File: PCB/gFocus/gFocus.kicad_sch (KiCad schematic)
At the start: 49 parts, among them J1 FTSH-105-01-F-DV-P-TR, J2 Conn_Coaxial, J3 Conn_02x06_Counter_Clockwise, J4 USB_B_Micro, U1 NMA0515SC, U2 TPS7A3001DGNT, U3 TPS7A4901DGNR, U4 AD5761RBRUZ-RL7, U5 ATSAMD21G18A-A, U6 IP4234CZ6, U8 LDK130-32_SOT23_SOT353

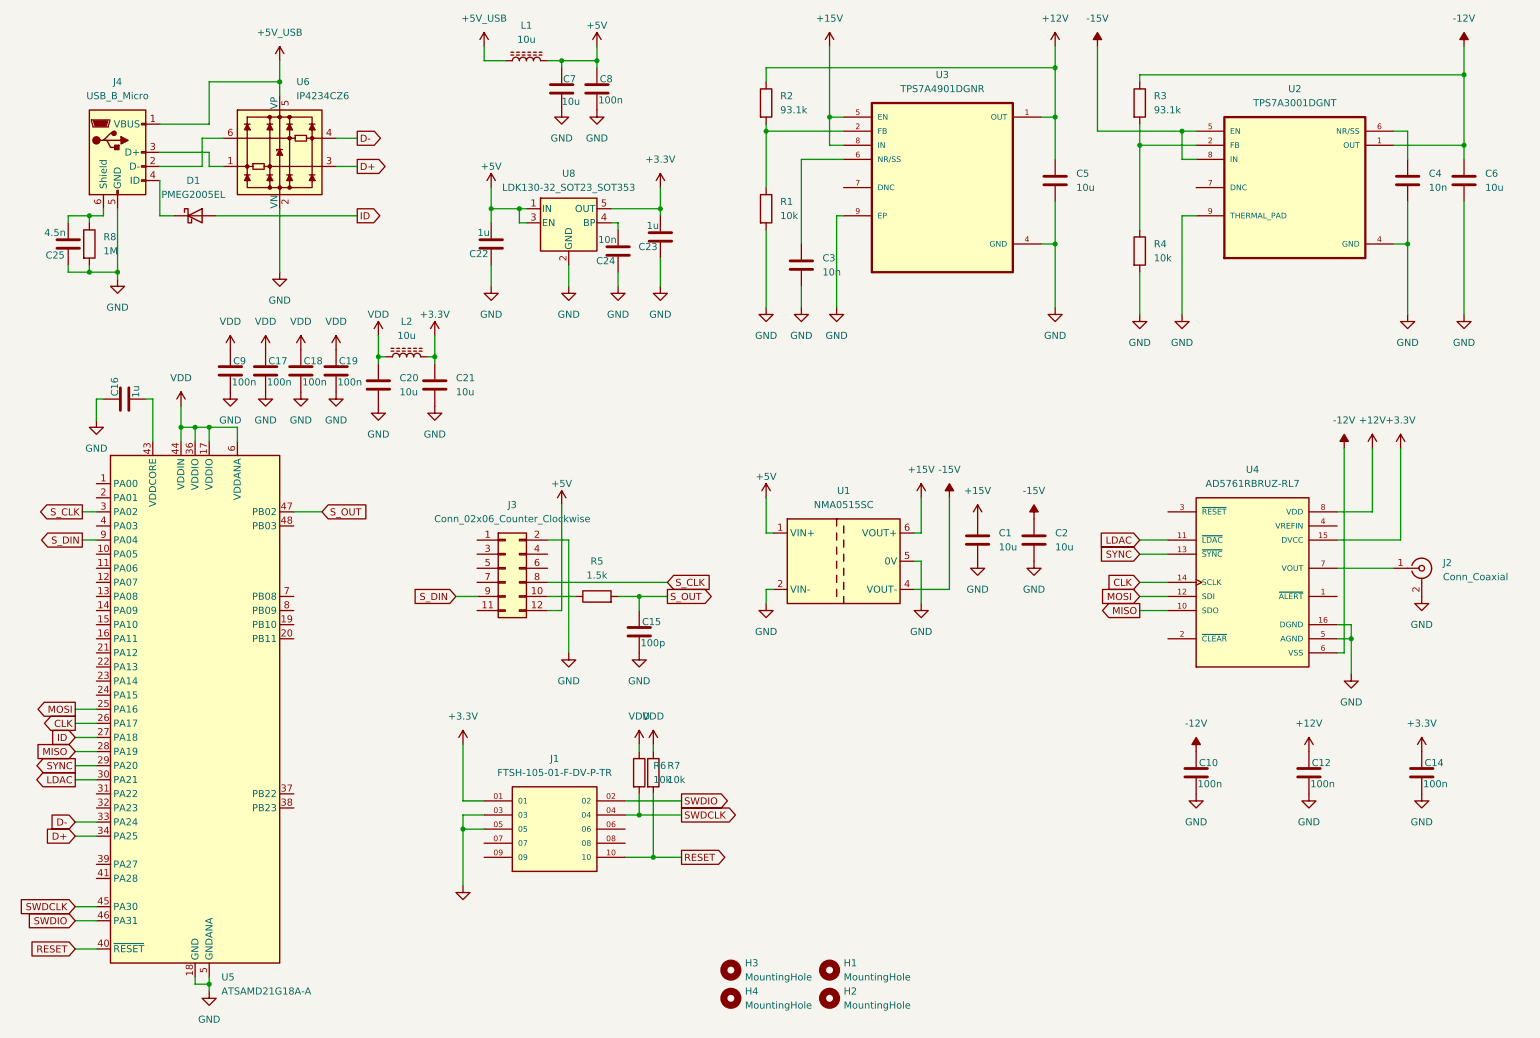
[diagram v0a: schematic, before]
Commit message: added drivers
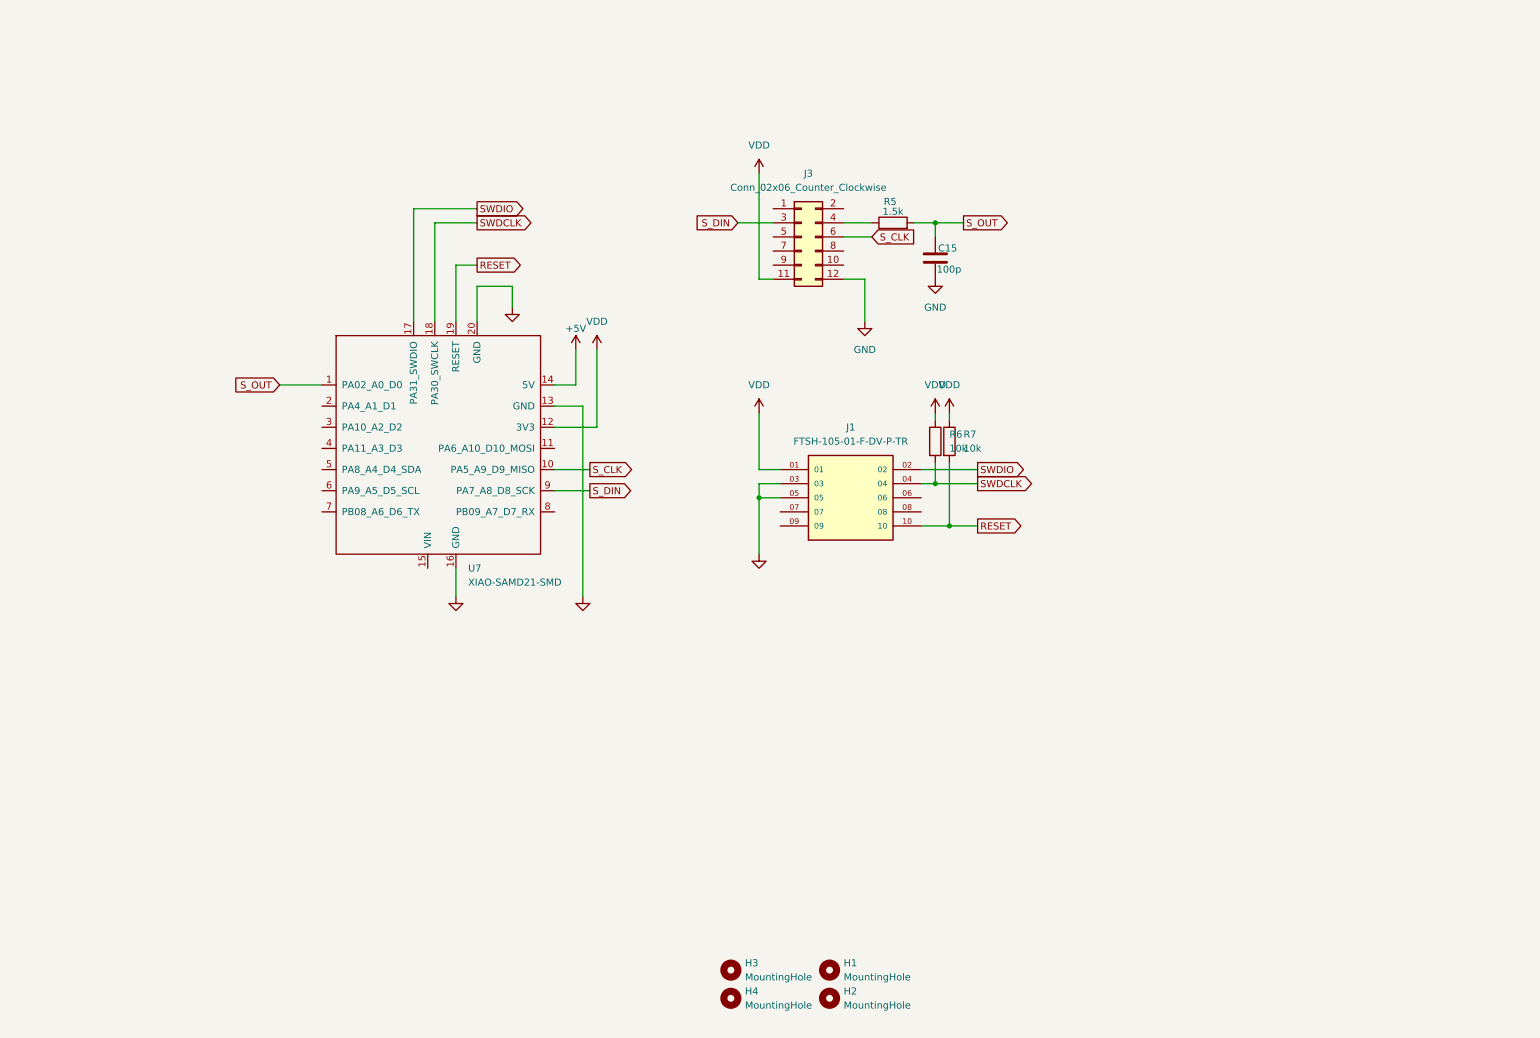
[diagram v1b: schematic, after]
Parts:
- removed C1, C2, C20, C21, C5, C6, C7: 10u, Capacitor_SMD:C_0805_2012Metric, symbol Device:C
- removed C10, C12, C14, C17, C18, C19, C8, C9: 100n, Capacitor_SMD:C_0805_2012Metric, symbol Device:C
- removed C16, C22, C23: 1u, Capacitor_SMD:C_0805_2012Metric, symbol Device:C
- removed C24, C3, C4: 10n, Capacitor_SMD:C_0805_2012Metric, symbol Device:C
- removed C25: 4.5n, Capacitor_SMD:C_0805_2012Metric, symbol Device:C
- removed D1: PMEG2005EL, Diode_SMD:D_SOD-882, symbol Device:D_Schottky
- removed J2: Conn_Coaxial, Connector_Coaxial:SMA_Amphenol_132289_EdgeMount, symbol Connector:Conn_Coaxial
- removed J4: USB_B_Micro, Connector_USB:USB_Micro-B_Molex-105017-0001, symbol Connector:USB_B_Micro
- removed L1, L2: 10u, Inductor_SMD:L_0805_2012Metric, symbol Device:L_Ferrite
- removed R1, R4: 10k, Resistor_SMD:R_0805_2012Metric, symbol Device:R
- removed R2, R3: 93.1k, Resistor_SMD:R_0805_2012Metric, symbol Device:R
- removed R8: 1M, Resistor_SMD:R_0805_2012Metric, symbol Device:R
- removed U1: NMA0515SC, Converter_DCDC:Converter_DCDC_Murata_NMAxxxxSC_THT, symbol Regulator_Switching:NMA0515SC
- removed U2: TPS7A3001DGNT, TPS7A3001DGNT:SOP65P490X110-9N, symbol TPS7A3001DGNT:TPS7A3001DGNT
- removed U3: TPS7A4901DGNR, TPS7A3001DGNT:SOP65P490X110-9N, symbol TPS7A4901DGNR:TPS7A4901DGNR
- removed U4: AD5761RBRUZ-RL7, AD5761RBRUZ-RL7:SOP65P640X120-16N, symbol AD5761RBRUZ-RL7:AD5761RBRUZ-RL7
- removed U5: ATSAMD21G18A-A, Package_QFP:TQFP-48_7x7mm_P0.5mm, symbol MCU_Microchip_SAMD:ATSAMD21G18A-A
- removed U6: IP4234CZ6, Package_TO_SOT_SMD:SOT-23-6, symbol Power_Protection:IP4234CZ6
- removed U8: LDK130-32_SOT23_SOT353, Package_TO_SOT_SMD:SOT-23-5_HandSoldering, symbol Regulator_Linear:LDK130-32_SOT23_SOT353
- added U7: XIAO-SAMD21-SMD, Seeed Studio XIAO Series Library:XIAO-SAMD21-SMD, symbol Seeed_Studio_XIAO_Series:XIAO-SAMD21-SMD
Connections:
- net +3.3V is gone; now on net VDD: J1.01
- net +5V: now also U7.14 (5V); no longer J3.12 (Pin_12)
- net GND: now also J3.12 (Pin_12), U7.13 (GND), U7.16 (GND), U7.20 (GND); no longer J3.2 (Pin_2)
- net RESET: now also U7.19 (RESET)
- net SWDCLK: now also U7.18 (PA30_SWCLK)
- net SWDIO: now also U7.17 (PA31_SWDIO)
- net S_CLK: now also J3.6 (Pin_6), U7.10 (PA5_A9_D9_MISO); no longer J3.8 (Pin_8)
- net S_DIN: now also J3.3 (Pin_3), U7.9 (PA7_A8_D8_SCK); no longer J3.9 (Pin_9)
- net S_OUT: now also U7.1 (PA02_A0_D0)
- net VDD: now also J3.11 (Pin_11), U7.12 (3V3)
- net at R5.1: now also J3.4 (Pin_4); no longer J3.10 (Pin_10)
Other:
- moved on the sheet: C15, J1, J3, R5, R6, R7
